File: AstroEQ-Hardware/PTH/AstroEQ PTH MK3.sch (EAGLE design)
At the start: 43 parts, among them IC1 ATMEGA162-16PU, IC2 PIC18F14K50-I/P, IC3 78L05, J1 POWER_JACKPTH, M1 Motor Driver, M2 Motor Driver, X1 16MHz, X2 12MHz

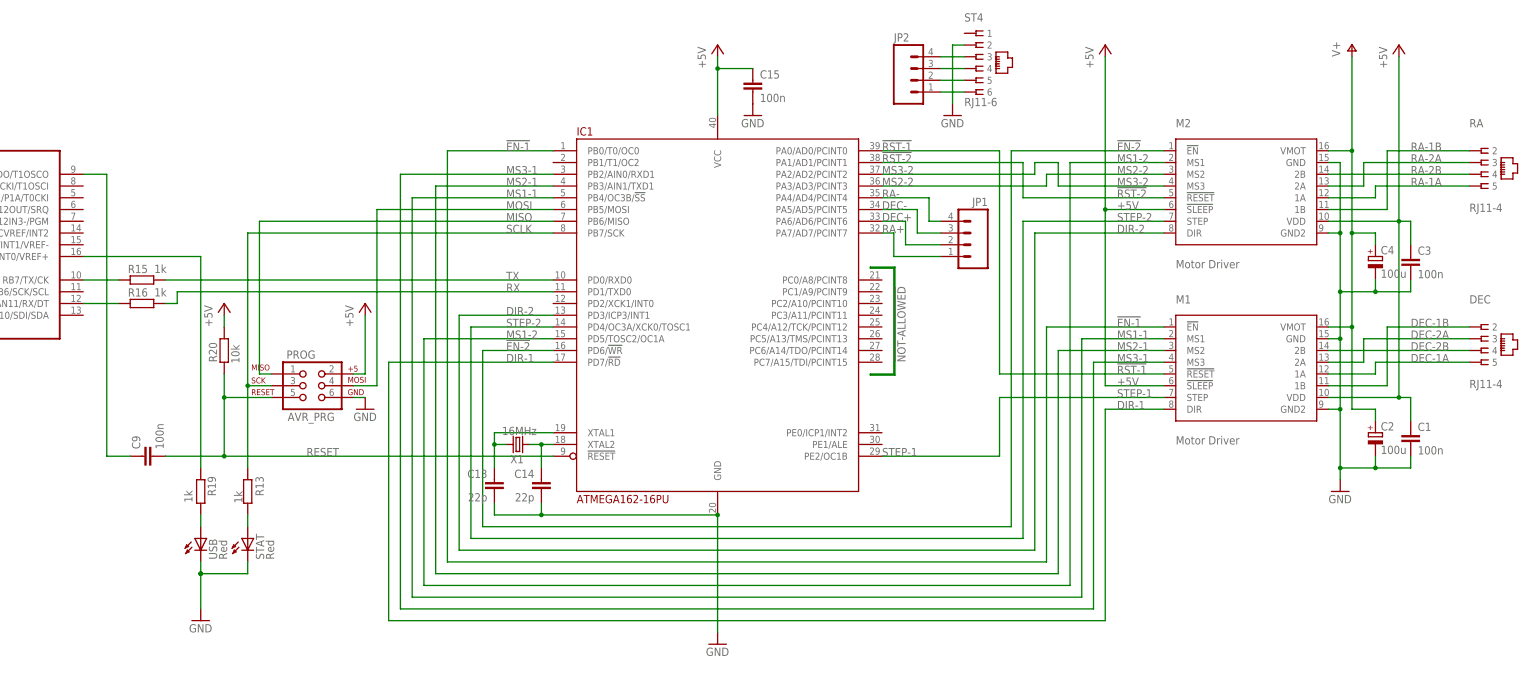
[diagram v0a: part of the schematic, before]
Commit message: Update DIY Eagle Designs
(1) Bring AstroEQ-DIY up to date (V4.4)
(2) Export AstroEQ-DIY schematic to PDF
(3) Make sure the etch file doesn't have holes in pads
(4) Add AstroEQ-ARD variant - Arduino Mega sheild
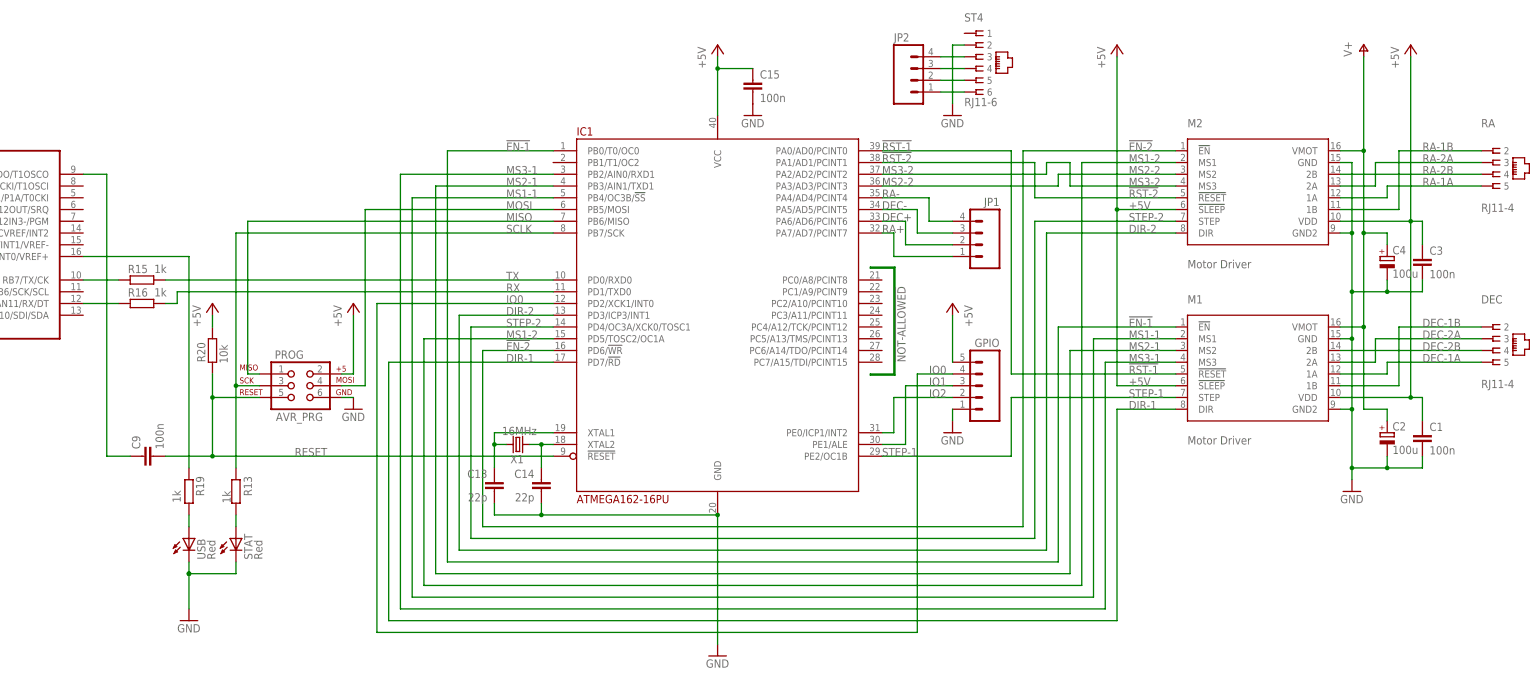
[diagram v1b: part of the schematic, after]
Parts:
- added GPIO: (no value), SparkFun:M05PTH
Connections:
- new net IO0: GPIO.4, IC1.PD2/XCK1/INT0
- new net IO1: GPIO.3, IC1.PE1/ALE
- new net IO2: GPIO.2, IC1.PE0/ICP1/INT2
- net +5V: now also GPIO.5
- net GND: now also GPIO.1
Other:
- moved on the sheet: C1, C2, C3, C4, DEC, JP1, M1, M2, PROG, R13, R19, R20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

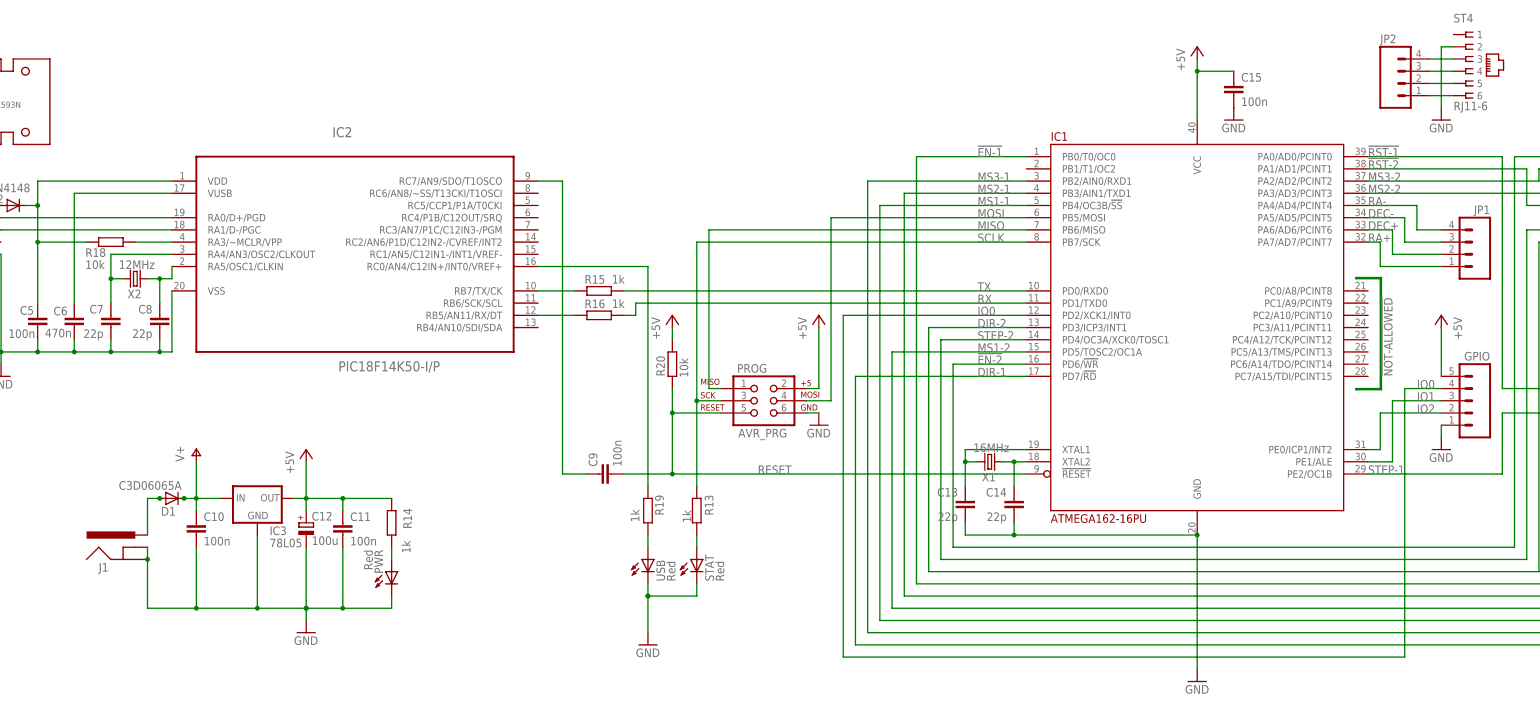
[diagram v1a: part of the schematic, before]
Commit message: Update PCB Logo
Add AstroEQ logo to PCB hardware designs.
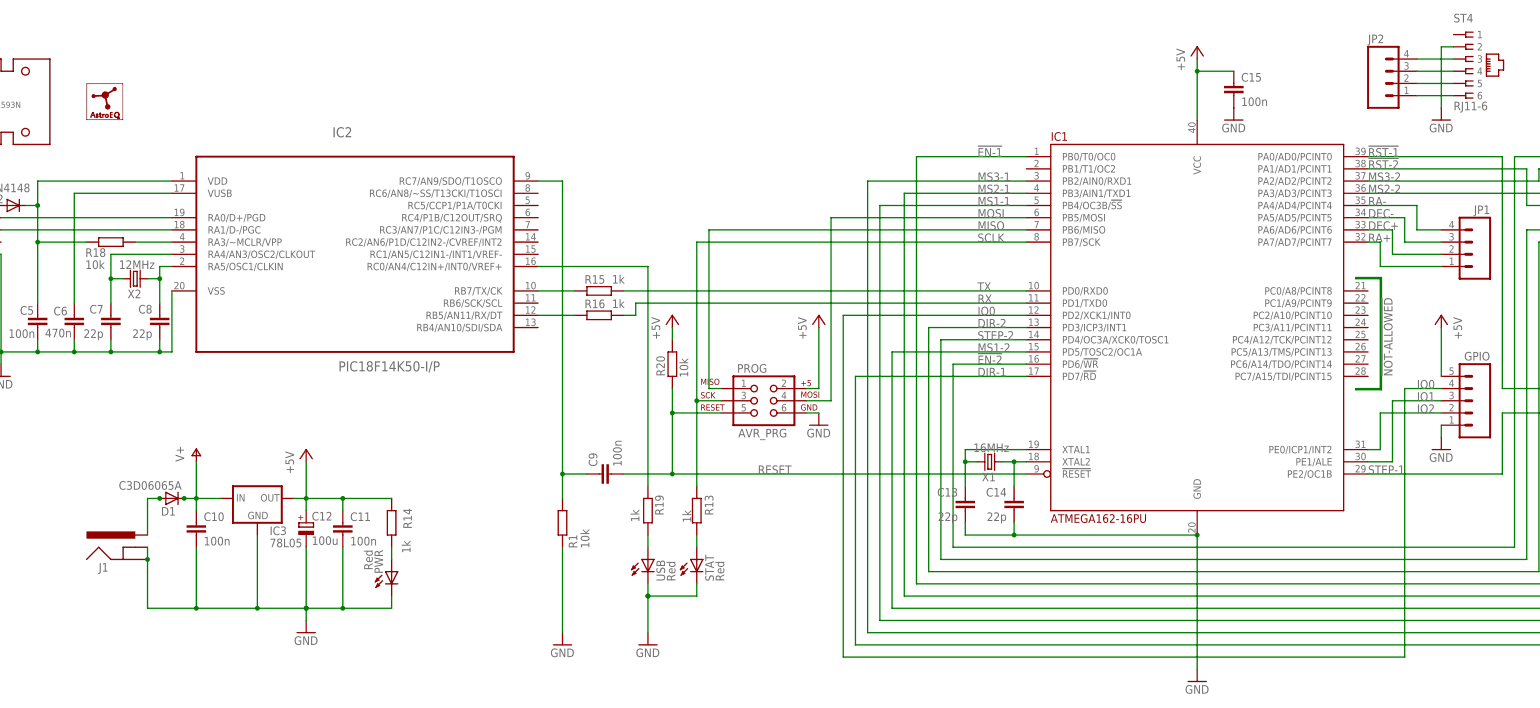
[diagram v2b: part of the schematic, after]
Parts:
- added LOGO1: ASTROEQ5MM, CompanyLogos:ASTROEQ5MM
- added R1: 10k, rcl:R-EU_0204/7
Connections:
- removed net DEC+B: JP2.2, ST4.5
- removed net DEC-B: JP2.3, ST4.4
- removed net RA+B: JP2.1, ST4.6
- removed net RA-B: JP2.4, ST4.3
- net DEC+: now also JP2.2, ST4.5
- net DEC-: now also JP2.3, ST4.4
- net DTR: now also R1.1
- net GND: now also R1.2
- net RA+: now also JP2.1, ST4.6
- net RA-: now also JP2.4, ST4.3
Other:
- moved on the sheet: JP2
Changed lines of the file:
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@@
 <?xml version="1.0" encoding="utf-8"?>
 <!DOCTYPE eagle SYSTEM "eagle.dtd">
-<eagle version="6.5.0">
+<eagle version="6.6.0">
 <drawing>
 <settings>
@@
 <layer number="110" name="fp0" color="7" fill="1" visible="no" active="yes"/>
 <layer number="111" name="LPC17xx" color="7" fill="1" visible="yes" active="yes"/>
+<layer number="112" name="tSilk" color="7" fill="1" visible="no" active="yes"/>
 <layer number="116" name="Patch_BOT" color="9" fill="4" visible="no" active="yes"/>
 <layer number="121" name="_tsilk" color="7" fill="1" visible="no" active="yes"/>
@@
 <layer number="124" name="bTestmark" color="7" fill="1" visible="no" active="yes"/>
 <layer number="125" name="_tNames" color="7" fill="1" visible="no" active="yes"/>
+<layer number="126" name="_bNames" color="7" fill="1" visible="no" active="yes"/>
+<layer number="127" name="_tValues" color="7" fill="1" visible="no" active="yes"/>
+<layer number="128" name="_bValues" color="7" fill="1" visible="no" active="yes"/>
 <layer number="131" name="tAdjust" color="7" fill="1" visible="no" active="yes"/>
 <layer number="132" name="bAdjust" color="7" fill="1" visible="no" active="yes"/>
 <layer number="144" name="Drill_legend" color="7" fill="1" visible="no" active="yes"/>
 <layer number="151" name="HeatSink" color="7" fill="1" visible="no" active="yes"/>
+<layer number="152" name="_bDocu" color="7" fill="1" visible="no" active="yes"/>
 <layer number="199" name="Contour" color="7" fill="1" visible="yes" active="yes"/>
 <layer number="200" name="200bmp" color="1" fill="10" visible="no" active="yes"/>
@@
 <layer number="223" name="223bmp" color="24" fill="1" visible="no" active="no"/>
 <layer number="224" name="224bmp" color="25" fill="1" visible="no" active="no"/>
+<layer number="248" name="Housing" color="7" fill="1" visible="no" active="yes"/>
+<layer number="249" name="Edge" color="7" fill="1" visible="no" active="yes"/>
 <layer number="250" name="Descript" color="3" fill="1" visible="no" active="no"/>
 <layer number="251" name="SMDround" color="12" fill="11" visible="no" active="no"/>
@@
 <part name="P+1" library="supply1" deviceset="+5V" device=""/>
 <part name="GND6" library="supply1" deviceset="GND" device=""/>
+<part name="R1" library="rcl" deviceset="R-EU_" device="0204/7" value="10k">
+<attribute name="MF" value="MULTICOMP"/>
+<attribute name="MPN" value="MF12 10K"/>
+<attribute name="OC_FARNELL" value="9342419"/>
+</part>
+<part name="GND7" library="supply1" deviceset="GND" device=""/>
+<part name="LOGO1" library="CompanyLogos" deviceset="ASTROEQ" device="5MM"/>
 </parts>
 <sheets>
@@
 <instance part="ST4" gate="G$1" x="317.5" y="266.7"/>
 <instance part="JP1" gate="G$1" x="317.5" y="226.06" rot="MR0"/>
-<instance part="JP2" gate="G$1" x="304.8" y="261.62"/>
+<instance part="JP2" gate="G$1" x="302.26" y="261.62"/>
 <instance part="GPIO" gate="G$1" x="320.04" y="195.58" rot="MR0"/>
 <instance part="P+1" gate="1" x="312.42" y="213.36" rot="MR0"/>
 <instance part="GND6" gate="1" x="312.42" y="185.42"/>
+<instance part="R1" gate="G$1" x="129.54" y="170.18" smashed="yes" rot="R270">
+<attribute name="NAME" x="132.6134" y="164.846" size="1.778" layer="95" rot="R90"/>
+<attribute name="VALUE" x="135.128" y="164.846" size="1.778" layer="96" rot="R90"/>
+<attribute name="OC_FARNELL" value="9342419" x="129.54" y="170.18" size="1.778" layer="96" rot="R90" display="off"/>
+<attribute name="MF" value="MULTICOMP" x="129.54" y="170.18" size="1.778" layer="96" rot="R90" display="off"/>
+<attribute name="MPN" value="MF12 10K" x="129.54" y="170.18" size="1.778" layer="96" rot="R90" display="off"/>
+</instance>
+<instance part="GND7" gate="1" x="129.54" y="144.78"/>
+<instance part="LOGO1" gate="G$1" x="30.48" y="254"/>
 </instances>
 <busses>
@@
 <wire x1="312.42" y1="190.5" x2="312.42" y2="187.96" width="0.1524" layer="91"/>
 </segment>
+<segment>
+<pinref part="R1" gate="G$1" pin="2"/>
+<pinref part="GND7" gate="1" pin="GND"/>
+<wire x1="129.54" y1="147.32" x2="129.54" y2="165.1" width="0.1524" layer="91"/>
+</segment>
 </net>
 <net name="V+" class="0">
@@
 <segment>
 <pinref part="IC2" gate="A" pin="RA5/OSC1/CLKIN"/>
-<wire x1="48.26" y1="223.52" x2="48.26" y2="220.98" width="0.1524" layer="91"/>
+<wire x1="48.26" y1="223.52" x2="45.72" y2="223.52" width="0.1524" layer="91"/>
 <pinref part="X2" gate="G$1" pin="1"/>
-<wire x1="48.26" y1="220.98" x2="45.72" y2="220.98" width="0.1524" layer="91"/>
+<wire x1="45.72" y1="223.52" x2="45.72" y2="220.98" width="0.1524" layer="91"/>
 <junction x="45.72" y="220.98"/>
 <wire x1="45.72" y1="220.98" x2="43.18" y2="220.98" width="0.1524" layer="91"/>
@@
 <wire x1="129.54" y1="180.34" x2="134.62" y2="180.34" width="0.1524" layer="91"/>
 <pinref part="C9" gate="G$1" pin="1"/>
+<pinref part="R1" gate="G$1" pin="1"/>
+<wire x1="129.54" y1="175.26" x2="129.54" y2="180.34" width="0.1524" layer="91"/>
+<junction x="129.54" y="180.34"/>
 </segment>
 </net>
@@
 <pinref part="JP1" gate="G$1" pin="1"/>
 </segment>
+<segment>
+<pinref part="ST4" gate="G$1" pin="6"/>
+<pinref part="JP2" gate="G$1" pin="1"/>
+<wire x1="307.34" y1="259.08" x2="314.96" y2="259.08" width="0.1524" layer="91"/>
+</segment>
 </net>
 <net name="DEC+" class="0">
@@
 <wire x1="312.42" y1="226.06" x2="302.26" y2="226.06" width="0.1524" layer="91"/>
 </segment>
+<segment>
+<pinref part="ST4" gate="G$1" pin="5"/>
+<pinref part="JP2" gate="G$1" pin="2"/>
+<wire x1="307.34" y1="261.62" x2="314.96" y2="261.62" width="0.1524" layer="91"/>
+</segment>
 </net>
 <net name="DEC-" class="0">
@@
 <wire x1="312.42" y1="228.6" x2="304.8" y2="228.6" width="0.1524" layer="91"/>
 </segment>
+<segment>
+<pinref part="ST4" gate="G$1" pin="4"/>
+<pinref part="JP2" gate="G$1" pin="3"/>
+<wire x1="307.34" y1="264.16" x2="314.96" y2="264.16" width="0.1524" layer="91"/>
+</segment>
 </net>
 <net name="RA-" class="0">
@@
 <wire x1="312.42" y1="231.14" x2="307.34" y2="231.14" width="0.1524" layer="91"/>
 </segment>
-</net>
-<net name="DEC+B" class="0">
-<segment>
-<pinref part="ST4" gate="G$1" pin="5"/>
-<pinref part="JP2" gate="G$1" pin="2"/>
-<wire x1="309.88" y1="261.62" x2="314.96" y2="261.62" width="0.1524" layer="91"/>
-</segment>
-</net>
-<net name="DEC-B" class="0">
-<segment>
-<pinref part="ST4" gate="G$1" pin="4"/>
-<pinref part="JP2" gate="G$1" pin="3"/>
-<wire x1="309.88" y1="264.16" x2="314.96" y2="264.16" width="0.1524" layer="91"/>
-</segment>
-</net>
-<net name="RA-B" class="0">
 <segment>
 <pinref part="ST4" gate="G$1" pin="3"/>
 <pinref part="JP2" gate="G$1" pin="4"/>
-<wire x1="309.88" y1="266.7" x2="314.96" y2="266.7" width="0.1524" layer="91"/>
-</segment>
-</net>
-<net name="RA+B" class="0">
-<segment>
-<pinref part="ST4" gate="G$1" pin="6"/>
-<pinref part="JP2" gate="G$1" pin="1"/>
-<wire x1="309.88" y1="259.08" x2="314.96" y2="259.08" width="0.1524" layer="91"/>
-</segment>
-</net>
+<wire x1="307.34" y1="266.7" x2="314.96" y2="266.7" width="0.1524" layer="91"/>
+</segment>
+</net>
